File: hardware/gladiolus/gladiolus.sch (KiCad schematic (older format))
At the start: 133 parts, among them J1 NEIGHBOR1, J2 NEIGHBOR2, J7 BONUS_ROW, P1 CONN_01X05, Q1 Q_NPN_BEC, U1 THS4520RGT, U2 AD8330ARQZ, U3 AD9283, U4 AD9704, U5 LMH6643

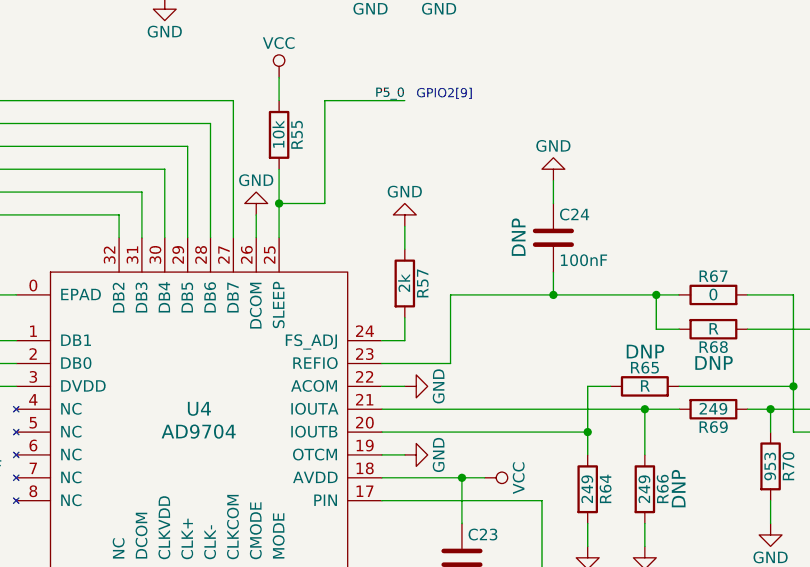
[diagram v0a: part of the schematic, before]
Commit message: Gladiolus: changed R57 from 2k to 20k to bring DAC output current into supported range
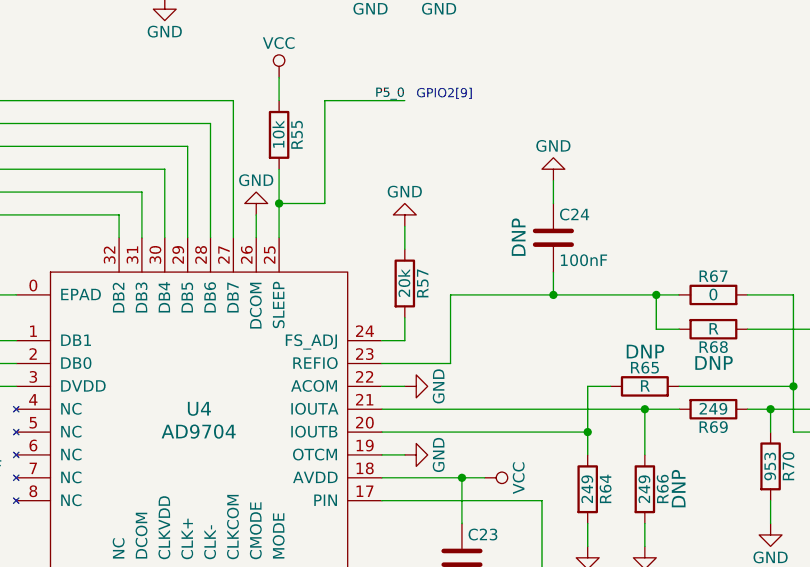
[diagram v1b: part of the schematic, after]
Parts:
- R57: value 2k -> 20k; Description RES SMD 2K OHM 5% 1/10W 0603 -> RES SMD 20K OHM 5% 1/10W 0603; Part Number 311-2.0KGR -> RC0603JR-0720KL
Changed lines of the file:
@@
 P 3950 6850
 F 0 "R57" V 4030 6850 50  0000 C CNN
-F 1 "2k" V 3950 6850 50  0000 C CNN
+F 1 "20k" V 3950 6850 50  0000 C CNN
 F 2 "gsg-modules:0603" V 3880 6850 50  0001 C CNN
 F 3 "" H 3950 6850 50  0000 C CNN
 F 4 "Yageo" H 3950 6850 60  0001 C CNN "Manufacturer"
-F 5 "311-2.0KGR" H 3950 6850 60  0001 C CNN "Part Number"
-F 6 "RES SMD 2K OHM 5% 1/10W 0603" H 3950 6850 60  0001 C CNN "Description"
+F 5 "RC0603JR-0720KL" H 3950 6850 60  0001 C CNN "Part Number"
+F 6 "RES SMD 20K OHM 5% 1/10W 0603" H 3950 6850 60  0001 C CNN "Description"
 	1    3950 6850
 	1    0    0    -1

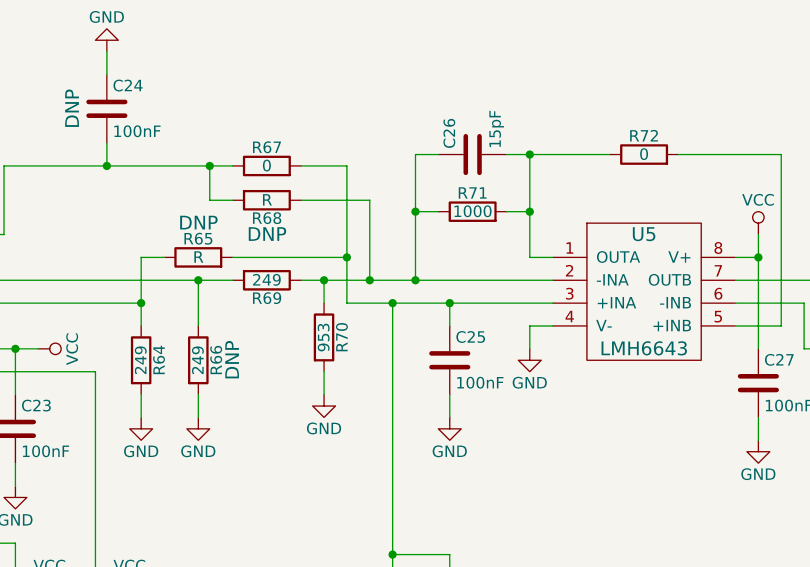
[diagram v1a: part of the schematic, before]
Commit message: Gladiolus: changed R70 and R71 values to shift common mode voltage of DAC amplifier output
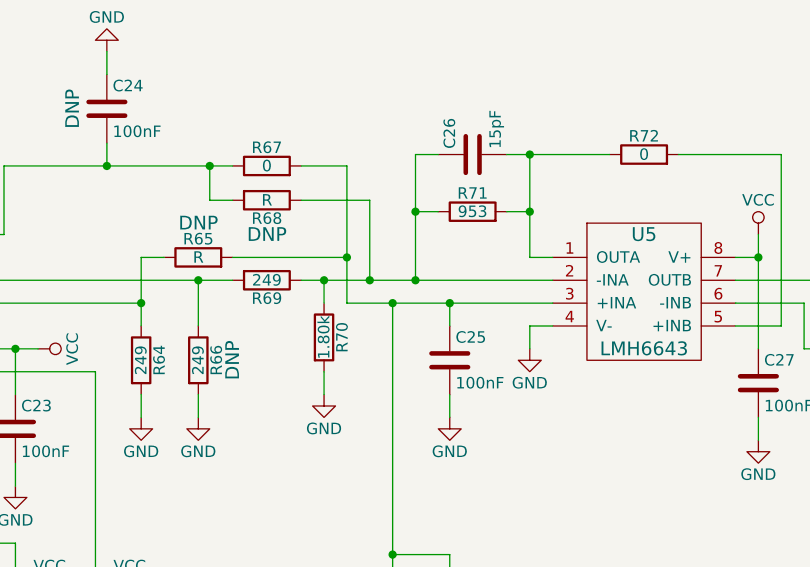
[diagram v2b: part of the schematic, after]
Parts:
- R70: value 953 -> 1.80k; Description RES SMD 953 OHM 1% 1/10W 0603 -> RES SMD 1.8K OHM 1% 1/10W 0603; Part Number RC0603FR-07953RL -> RC0603FR-071K8L
- R71: value 1000 -> 953; Description RES SMD 1K OHM 5% 1/10W 0603 -> RES SMD 953 OHM 1% 1/10W 0603; Part Number 311-1.0KGR -> RC0603FR-07953RL
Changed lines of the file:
@@
 P 6200 7100
 F 0 "R71" V 6280 7100 50  0000 C CNN
-F 1 "1000" V 6200 7100 50  0000 C CNN
+F 1 "953" V 6200 7100 50  0000 C CNN
 F 2 "gsg-modules:0603" V 6130 7100 50  0001 C CNN
 F 3 "" H 6200 7100 50  0000 C CNN
 F 4 "Yageo" H 6200 7100 60  0001 C CNN "Manufacturer"
-F 5 "311-1.0KGR" H 6200 7100 60  0001 C CNN "Part Number"
-F 6 "RES SMD 1K OHM 5% 1/10W 0603" H 6200 7100 60  0001 C CNN "Description"
+F 5 "RC0603FR-07953RL" H 6200 7100 60  0001 C CNN "Part Number"
+F 6 "RES SMD 953 OHM 1% 1/10W 0603" H 6200 7100 60  0001 C CNN "Description"
 	1    6200 7100
 	0    -1   -1   0
@@
 P 5550 7650
 F 0 "R70" V 5630 7650 50  0000 C CNN
-F 1 "953" V 5550 7650 50  0000 C CNN
+F 1 "1.80k" V 5550 7650 50  0000 C CNN
 F 2 "gsg-modules:0603" V 5480 7650 50  0001 C CNN
 F 3 "" H 5550 7650 50  0000 C CNN
 F 4 "Yageo" H 5550 7650 60  0001 C CNN "Manufacturer"
-F 5 "RC0603FR-07953RL" H 5550 7650 60  0001 C CNN "Part Number"
-F 6 "RES SMD 953 OHM 1% 1/10W 0603" H 5550 7650 60  0001 C CNN "Description"
+F 5 "RC0603FR-071K8L" H 5550 7650 60  0001 C CNN "Part Number"
+F 6 "RES SMD 1.8K OHM 1% 1/10W 0603" H 5550 7650 60  0001 C CNN "Description"
 	1    5550 7650
 	1    0    0    -1

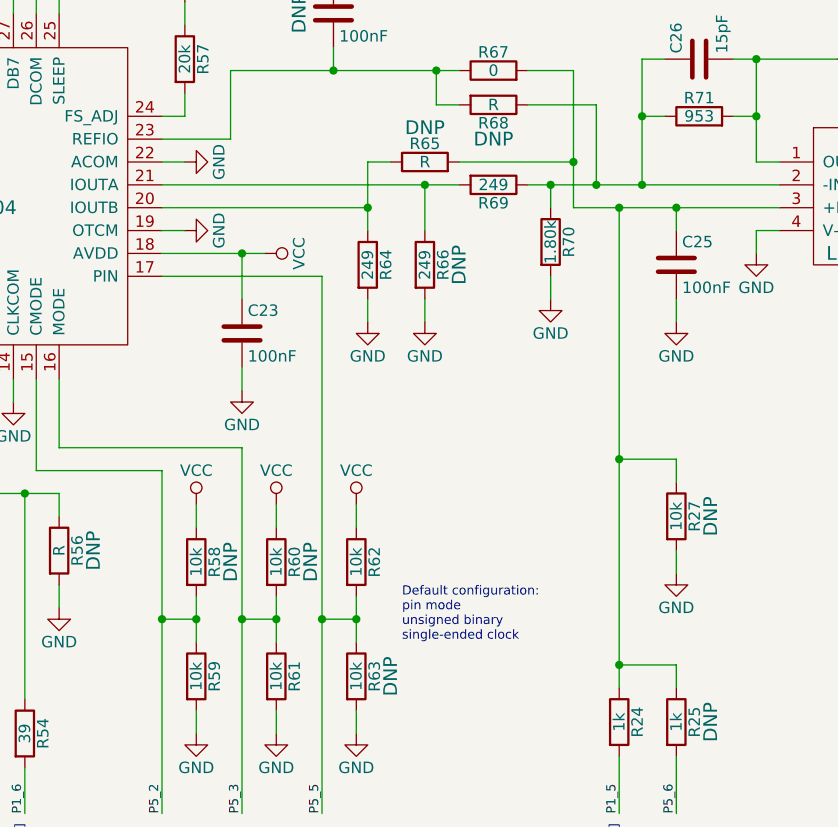
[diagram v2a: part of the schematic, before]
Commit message: Gladiolus: inverted DAC output by swapping differential output pin connections
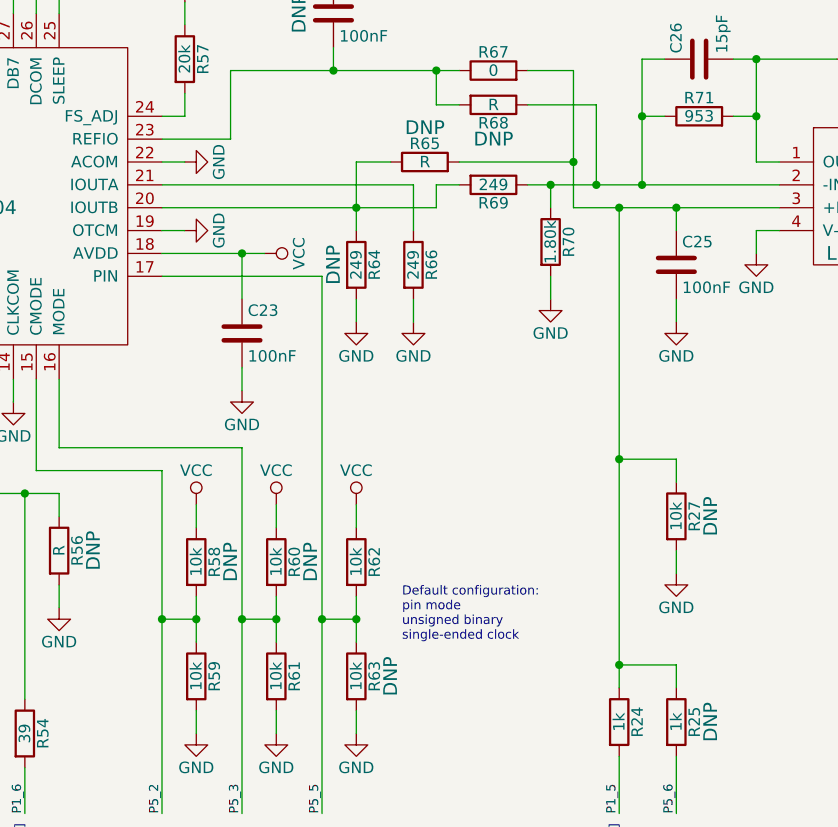
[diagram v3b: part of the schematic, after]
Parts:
- R64: Note (none) -> DNP
- R66: Note DNP -> (none)
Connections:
- net at R64.1, R65.1, U4.20 (IOUTB): now also R69.2
- net at R66.1, U4.21 (IOUTA): no longer R69.2
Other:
- moved on the sheet: R64, R66
